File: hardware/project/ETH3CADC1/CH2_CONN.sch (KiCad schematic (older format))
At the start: 1 part, among them J1101 Conn_02x10_Odd_Even

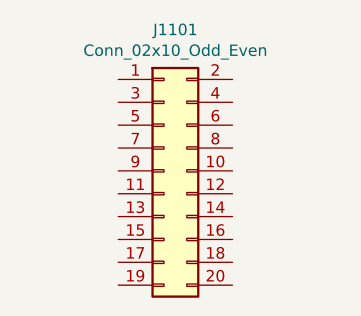
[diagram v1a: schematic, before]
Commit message: SDRAM works, thanks to the website https://medium.com/@pjinwoo123/stm32h7-external-sdram-evaluation-board-cc72444898d8 . Modified the code to work with SDRAM BANK2. SCPI library works.
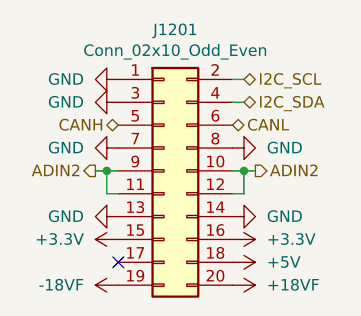
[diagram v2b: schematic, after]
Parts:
- renumbered J1101 to J1201
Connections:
- net GND: now reaches J1201.1 (Pin_1)
- net GND: now also J1201.13 (Pin_13), J1201.14 (Pin_14), J1201.3 (Pin_3), J1201.7 (Pin_7), J1201.8 (Pin_8)
- net ADIN2: now reaches J1201.10 (Pin_10)
- net ADIN2: now also J1201.11 (Pin_11), J1201.12 (Pin_12), J1201.9 (Pin_9)
- net +3V3: now reaches J1201.15 (Pin_15)
- net +3V3: now also J1201.16 (Pin_16)
- net +5V: now reaches J1201.18 (Pin_18)
- net -18VF: now reaches J1201.19 (Pin_19)
- net I2C_SCL: now reaches J1201.2 (Pin_2)
- net +18VF: now reaches J1201.20 (Pin_20)
- net I2C_SDA: now reaches J1201.4 (Pin_4)
- net CANH: now reaches J1201.5 (Pin_5)
- net CANL: now reaches J1201.6 (Pin_6)
- no-connect marks 0 -> 1
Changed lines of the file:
@@
 $Descr A4 11693 8268
 encoding utf-8
-Sheet 11 15
+Sheet 12 13
 Title ""
 Date ""
@@
 P 5550 3500
 AR Path="/60C206FB/60C25971" Ref="J?"  Part="1"
-AR Path="/60C24B76/60C25971" Ref="J1101"  Part="1"
-F 0 "J1101" H 5600 4117 50  0000 C CNN
+AR Path="/60C24B76/60C25971" Ref="J1201"  Part="1"
+F 0 "J1201" H 5600 4117 50  0000 C CNN
 F 1 "Conn_02x10_Odd_Even" H 5600 4026 50  0000 C CNN
 F 2 "Connector_PinSocket_2.54mm:PinSocket_2x10_P2.54mm_Vertical" H 5550 3500 50  0001 C CNN
@@
 	1    0    0    -1
 $EndComp
+Text HLabel 5900 3100 2    50   BiDi ~ 0
+I2C_SCL
+Text HLabel 5900 3200 2    50   BiDi ~ 0
+I2C_SDA
+Wire Wire Line
+	5900 3100 5850 3100
+Wire Wire Line
+	5850 3200 5900 3200
+$Comp
+L power:GND #PWR01201
+U 1 1 60608795
+P 5350 3100
+F 0 "#PWR01201" H 5350 2850 50  0001 C CNN
+F 1 "GND" V 5350 2950 50  0000 R CNN
+F 2 "" H 5350 3100 50  0001 C CNN
+F 3 "" H 5350 3100 50  0001 C CNN
+	1    5350 3100
+	0    1    1    0
+$EndComp
+$Comp
+L power:GND #PWR01202
+U 1 1 60608DEE
+P 5350 3200
+F 0 "#PWR01202" H 5350 2950 50  0001 C CNN
+F 1 "GND" V 5350 3050 50  0000 R CNN
+F 2 "" H 5350 3200 50  0001 C CNN
+F 3 "" H 5350 3200 50  0001 C CNN
+	1    5350 3200
+	0    1    1    0
+$EndComp
+$Comp
+L power:GND #PWR01203
+U 1 1 6060A766
+P 5350 3400
+F 0 "#PWR01203" H 5350 3150 50  0001 C CNN
+F 1 "GND" V 5350 3250 50  0000 R CNN
+F 2 "" H 5350 3400 50  0001 C CNN
+F 3 "" H 5350 3400 50  0001 C CNN
+	1    5350 3400
+	0    1    1    0
+$EndComp
+$Comp
+L power:GND #PWR01207
+U 1 1 6060A9F3
+P 5850 3400
+F 0 "#PWR01207" H 5850 3150 50  0001 C CNN
+F 1 "GND" V 5850 3250 50  0000 R CNN
+F 2 "" H 5850 3400 50  0001 C CNN
+F 3 "" H 5850 3400 50  0001 C CNN
+	1    5850 3400
+	0    -1   -1   0
+$EndComp
+Wire Wire Line
+	5350 3600 5300 3600
+Wire Wire Line
+	5300 3600 5300 3500
+Wire Wire Line
+	5300 3500 5350 3500
+Wire Wire Line
+	5850 3600 5900 3600
+Wire Wire Line
+	5900 3600 5900 3500
+Wire Wire Line
+	5900 3500 5850 3500
+$Comp
+L power:GND #PWR01204
+U 1 1 6060B72E
+P 5350 3700
+F 0 "#PWR01204" H 5350 3450 50  0001 C CNN
+F 1 "GND" V 5350 3550 50  0000 R CNN
+F 2 "" H 5350 3700 50  0001 C CNN
+F 3 "" H 5350 3700 50  0001 C CNN
+	1    5350 3700
+	0    1    1    0
+$EndComp
+$Comp
+L power:GND #PWR01208
+U 1 1 6060BA4B
+P 5850 3700
+F 0 "#PWR01208" H 5850 3450 50  0001 C CNN
+F 1 "GND" V 5850 3550 50  0000 R CNN
+F 2 "" H 5850 3700 50  0001 C CNN
+F 3 "" H 5850 3700 50  0001 C CNN
+	1    5850 3700
+	0    -1   -1   0
+$EndComp
+$Comp
+L power:+3.3V #PWR01209
+U 1 1 6060D71C
+P 5850 3800
+F 0 "#PWR01209" H 5850 3650 50  0001 C CNN
+F 1 "+3.3V" V 5850 3950 50  0000 L CNN
+F 2 "" H 5850 3800 50  0001 C CNN
+F 3 "" H 5850 3800 50  0001 C CNN
+	1    5850 3800
+	0    1    1    0
+$EndComp
+$Comp
+L power:+3.3V #PWR01205
+U 1 1 6060DFE5
+P 5350 3800
+F 0 "#PWR01205" H 5350 3650 50  0001 C CNN
+F 1 "+3.3V" V 5350 3950 50  0000 L CNN
+F 2 "" H 5350 3800 50  0001 C CNN
+F 3 "" H 5350 3800 50  0001 C CNN
+	1    5350 3800
+	0    -1   -1   0
+$EndComp
+$Comp
+L power:+5V #PWR01210
+U 1 1 6060E900
+P 5850 3900
+F 0 "#PWR01210" H 5850 3750 50  0001 C CNN
+F 1 "+5V" V 5850 4050 50  0000 L CNN
+F 2 "" H 5850 3900 50  0001 C CNN
+F 3 "" H 5850 3900 50  0001 C CNN
+	1    5850 3900
+	0    1    1    0
+$EndComp
+$Comp
+L ETH3CDAQ1:-18VF #PWR01206
+U 1 1 60611488
+P 5350 4000
+F 0 "#PWR01206" H 5350 3850 50  0001 C CNN
+F 1 "-18VF" V 5350 4150 50  0000 L CNN
+F 2 "" H 5350 4000 50  0001 C CNN
+F 3 "" H 5350 4000 50  0001 C CNN
+	1    5350 4000
+	0    -1   -1   0
+$EndComp
+NoConn ~ 5350 3900
+$Comp
+L ETH3CDAQ1:+18VF #PWR01211
+U 1 1 60612313
+P 5850 4000
+F 0 "#PWR01211" H 5850 3850 50  0001 C CNN
+F 1 "+18VF" V 5850 4150 50  0000 L CNN
+F 2 "" H 5850 4000 50  0001 C CNN
+F 3 "" H 5850 4000 50  0001 C CNN
+	1    5850 4000
+	0    1    1    0
+$EndComp
+Text HLabel 5350 3300 0    50   BiDi ~ 0
+CANH
+Text HLabel 5850 3300 2    50   BiDi ~ 0
+CANL
+Text HLabel 5250 3500 0    50   Output ~ 0
+ADIN2
+Wire Wire Line
+	5250 3500 5300 3500
+Connection ~ 5300 3500
+Text HLabel 5950 3500 2    50   Output ~ 0
+ADIN2
+Wire Wire Line
+	5950 3500 5900 3500
+Connection ~ 5900 3500
 $EndSCHEMATC

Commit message: Development
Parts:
- renumbered J1201 to J1501
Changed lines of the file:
@@
 $Descr A4 11693 8268
 encoding utf-8
-Sheet 12 13
+Sheet 12 17
 Title ""
 Date ""
@@
 P 5550 3500
 AR Path="/60C206FB/60C25971" Ref="J?"  Part="1"
-AR Path="/60C24B76/60C25971" Ref="J1201"  Part="1"
-F 0 "J1201" H 5600 4117 50  0000 C CNN
+AR Path="/60C24B76/60C25971" Ref="J1501"  Part="1"
+F 0 "J1501" H 5600 4117 50  0000 C CNN
 F 1 "Conn_02x10_Odd_Even" H 5600 4026 50  0000 C CNN
 F 2 "Connector_PinSocket_2.54mm:PinSocket_2x10_P2.54mm_Vertical" H 5550 3500 50  0001 C CNN
@@
 	5850 3200 5900 3200
 $Comp
-L power:GND #PWR01201
+L power:GND #PWR01501
 U 1 1 60608795
 P 5350 3100
-F 0 "#PWR01201" H 5350 2850 50  0001 C CNN
+F 0 "#PWR01501" H 5350 2850 50  0001 C CNN
 F 1 "GND" V 5350 2950 50  0000 R CNN
 F 2 "" H 5350 3100 50  0001 C CNN
@@
 $EndComp
 $Comp
-L power:GND #PWR01202
+L power:GND #PWR01502
 U 1 1 60608DEE
 P 5350 3200
-F 0 "#PWR01202" H 5350 2950 50  0001 C CNN
+F 0 "#PWR01502" H 5350 2950 50  0001 C CNN
 F 1 "GND" V 5350 3050 50  0000 R CNN
 F 2 "" H 5350 3200 50  0001 C CNN
@@
 $EndComp
 $Comp
-L power:GND #PWR01203
+L power:GND #PWR01503
 U 1 1 6060A766
 P 5350 3400
-F 0 "#PWR01203" H 5350 3150 50  0001 C CNN
+F 0 "#PWR01503" H 5350 3150 50  0001 C CNN
 F 1 "GND" V 5350 3250 50  0000 R CNN
 F 2 "" H 5350 3400 50  0001 C CNN
@@
 $EndComp
 $Comp
-L power:GND #PWR01207
+L power:GND #PWR01507
 U 1 1 6060A9F3
 P 5850 3400
-F 0 "#PWR01207" H 5850 3150 50  0001 C CNN
+F 0 "#PWR01507" H 5850 3150 50  0001 C CNN
 F 1 "GND" V 5850 3250 50  0000 R CNN
 F 2 "" H 5850 3400 50  0001 C CNN
@@
 	5900 3500 5850 3500
 $Comp
-L power:GND #PWR01204
+L power:GND #PWR01504
 U 1 1 6060B72E
 P 5350 3700
-F 0 "#PWR01204" H 5350 3450 50  0001 C CNN
+F 0 "#PWR01504" H 5350 3450 50  0001 C CNN
 F 1 "GND" V 5350 3550 50  0000 R CNN
 F 2 "" H 5350 3700 50  0001 C CNN
@@
 $EndComp
 $Comp
-L power:GND #PWR01208
+L power:GND #PWR01508
 U 1 1 6060BA4B
 P 5850 3700
-F 0 "#PWR01208" H 5850 3450 50  0001 C CNN
+F 0 "#PWR01508" H 5850 3450 50  0001 C CNN
 F 1 "GND" V 5850 3550 50  0000 R CNN
 F 2 "" H 5850 3700 50  0001 C CNN
@@
 $EndComp
 $Comp
-L power:+3.3V #PWR01209
+L power:+3.3V #PWR01509
 U 1 1 6060D71C
 P 5850 3800
-F 0 "#PWR01209" H 5850 3650 50  0001 C CNN
+F 0 "#PWR01509" H 5850 3650 50  0001 C CNN
 F 1 "+3.3V" V 5850 3950 50  0000 L CNN
 F 2 "" H 5850 3800 50  0001 C CNN
@@
 $EndComp
 $Comp
-L power:+3.3V #PWR01205
+L power:+3.3V #PWR01505
 U 1 1 6060DFE5
 P 5350 3800
-F 0 "#PWR01205" H 5350 3650 50  0001 C CNN
+F 0 "#PWR01505" H 5350 3650 50  0001 C CNN
 F 1 "+3.3V" V 5350 3950 50  0000 L CNN
 F 2 "" H 5350 3800 50  0001 C CNN
@@
 $EndComp
 $Comp
-L power:+5V #PWR01210
+L power:+5V #PWR01510
 U 1 1 6060E900
 P 5850 3900
-F 0 "#PWR01210" H 5850 3750 50  0001 C CNN
+F 0 "#PWR01510" H 5850 3750 50  0001 C CNN
 F 1 "+5V" V 5850 4050 50  0000 L CNN
 F 2 "" H 5850 3900 50  0001 C CNN
@@
 $EndComp
 $Comp
-L ETH3CDAQ1:-18VF #PWR01206
+L ETH3CDAQ1:-18VF #PWR01506
 U 1 1 60611488
 P 5350 4000
-F 0 "#PWR01206" H 5350 3850 50  0001 C CNN
+F 0 "#PWR01506" H 5350 3850 50  0001 C CNN
 F 1 "-18VF" V 5350 4150 50  0000 L CNN
 F 2 "" H 5350 4000 50  0001 C CNN
@@
 NoConn ~ 5350 3900
 $Comp
-L ETH3CDAQ1:+18VF #PWR01211
+L ETH3CDAQ1:+18VF #PWR01511
 U 1 1 60612313
 P 5850 4000
-F 0 "#PWR01211" H 5850 3850 50  0001 C CNN
+F 0 "#PWR01511" H 5850 3850 50  0001 C CNN
 F 1 "+18VF" V 5850 4150 50  0000 L CNN
 F 2 "" H 5850 4000 50  0001 C CNN
